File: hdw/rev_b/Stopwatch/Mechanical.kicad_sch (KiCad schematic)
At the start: 12 parts

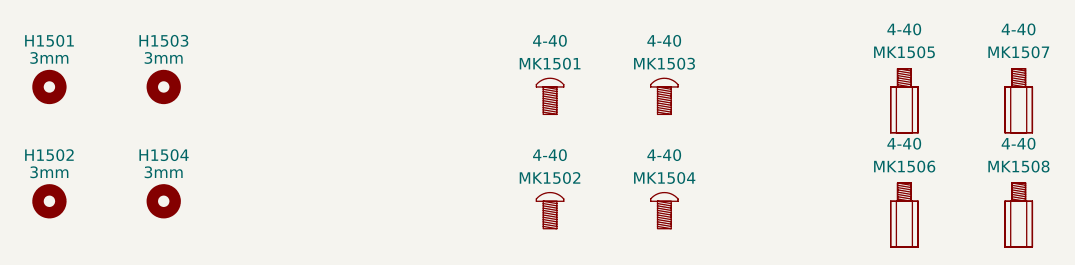
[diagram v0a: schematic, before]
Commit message: ported rev b to kicad 8
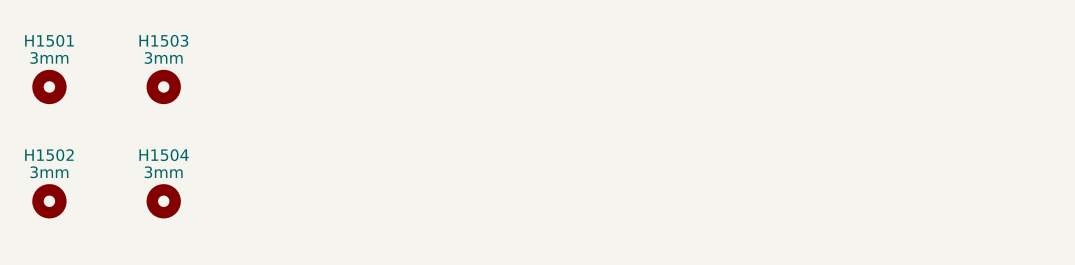
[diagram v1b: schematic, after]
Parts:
- removed MK1501, MK1502, MK1503, MK1504: 4-40, symbol Custom_Library:Screw
- removed MK1505, MK1506, MK1507, MK1508: 4-40, symbol Custom_Library:Standoff
